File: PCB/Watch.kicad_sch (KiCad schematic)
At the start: 47 parts, among them J1 USB_C_Receptacle_USB2.0_14P, Q1 2N3904, Q2 2N3904, Q3 2N3904, Q4 2N3904, SW1 SW_Push, SW3 SW_Push, SW4 SW_Push, U1 MCP73831-2-OT, U3 AP2112K-3.3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

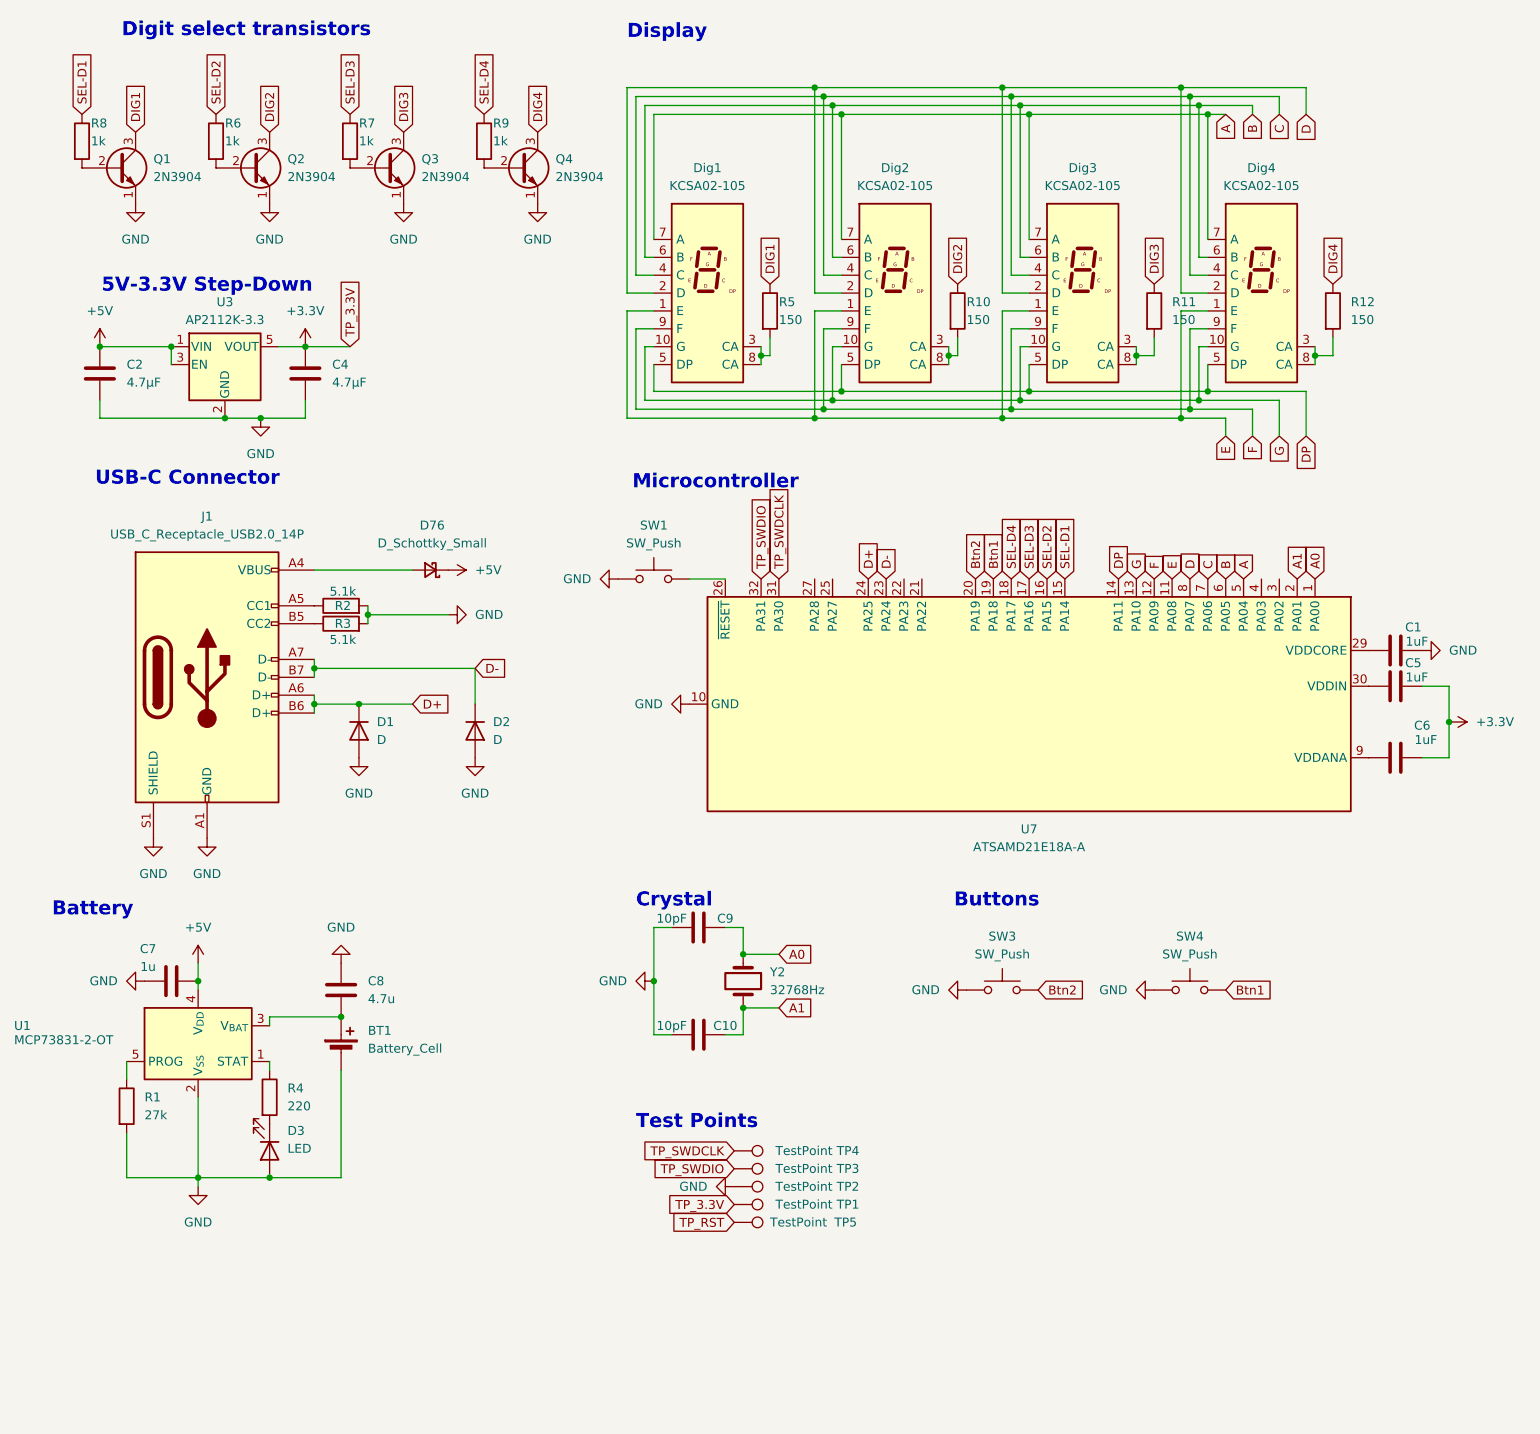
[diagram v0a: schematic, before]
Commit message: Switch regulator
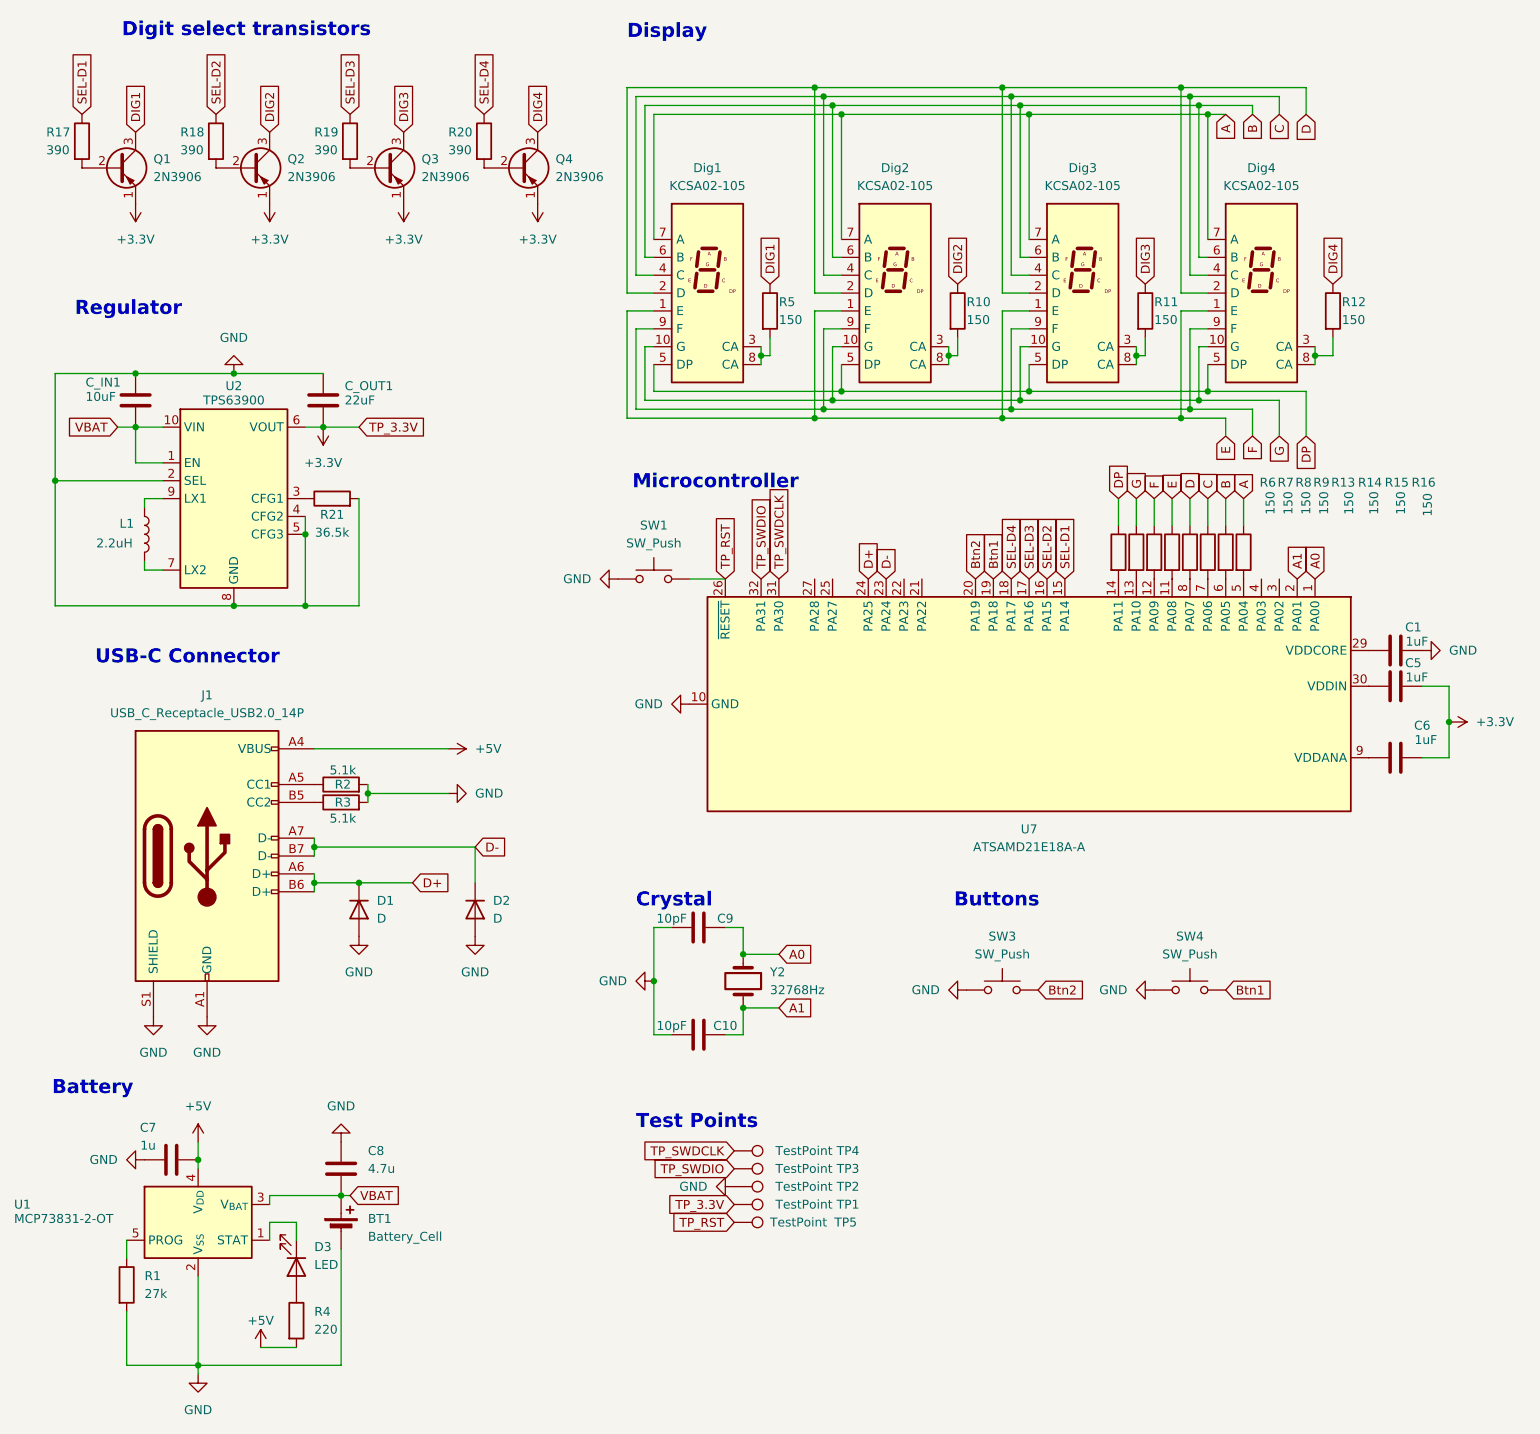
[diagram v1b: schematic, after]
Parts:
- removed C2, C4: 4.7µF, Capacitor_SMD:C_0603_1608Metric, symbol Device:C
- removed D76: D_Schottky_Small, Diode_SMD:D_SOD-323, symbol Device:D_Schottky_Small
- removed Q1, Q2, Q3, Q4: 2N3904, Package_TO_SOT_SMD:SOT-23, symbol Transistor_BJT:2N3904
- removed U3: AP2112K-3.3, Package_TO_SOT_SMD:SOT-23-5, symbol Regulator_Linear:AP2112K-3.3
- added C_IN1: 10uF, Capacitor_SMD:C_0603_1608Metric, symbol Device:C
- added C_OUT1: 22uF, Capacitor_SMD:C_0603_1608Metric, symbol Device:C
- added L1: 2.2uH, Inductor_SMD:L_0805_2012Metric, symbol Device:L
- added Q1, Q2, Q3, Q4: 2N3906, Package_TO_SOT_SMD:SOT-23, symbol Transistor_BJT:2N3906
- added R13, R14, R15, R16: 150, Resistor_SMD:R_0402_1005Metric, symbol Device:R
- added R17, R18, R19, R20: 390, Resistor_SMD:R_0402_1005Metric, symbol Device:R
- added R21: 36.5k, Resistor_SMD:R_0402_1005Metric, symbol Device:R
- added U2: TPS63900, Package_SON:WSON-10-1EP_2.5x2.5mm_P0.5mm_EP1.2x2mm_ThermalVias, symbol Regulator_Switching:TPS63900
- C1, C10, C5, C6, C7, C9: footprint Capacitor_SMD:C_0603_1608Metric -> Capacitor_SMD:C_0402_1005Metric
- D3: footprint LED_SMD:LED_0603_1608Metric -> LED_SMD:LED_0402_1005Metric
- R1, R10, R11, R12, R2, R3, R4, R5: footprint Resistor_SMD:R_0603_1608Metric -> Resistor_SMD:R_0402_1005Metric
- R6, R7, R8, R9: value 1k -> 150; footprint Resistor_SMD:R_0603_1608Metric -> Resistor_SMD:R_0402_1005Metric
- TP5: footprint (none) -> TestPoint:TestPoint_Pad_D1.0mm
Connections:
- net +3.3V: now also C_OUT1.2, Q1.1 (E), Q2.1 (E), Q3.1 (E), Q4.1 (E), U2.6 (VOUT)
- net +5V: now also J1.A4 (VBUS), J1.A9 (VBUS), J1.B4 (VBUS), J1.B9 (VBUS), R4.2
- net A: now also R16.1; no longer U7.5 (PA04)
- net B: now also R15.1; no longer U7.6 (PA05)
- net C: now also R14.1; no longer U7.7 (PA06)
- net D: now also R13.1; no longer U7.8 (PA07)
- net DIG1: now also Q1.3 (C)
- net DIG2: now also Q2.3 (C)
- net DIG3: now also Q3.3 (C)
- net DIG4: now also Q4.3 (C)
- net DP: now also R6.1; no longer U7.14 (PA11)
- net E: now also R9.1; no longer U7.11 (PA08)
- net F: now also R8.1; no longer U7.12 (PA09)
- net G: now also R7.1; no longer U7.13 (PA10)
- net GND: now also C_IN1.1, C_OUT1.1, R21.2, U2.11 (GND), U2.2 (SEL), U2.4 (CFG2), U2.5 (CFG3), U2.8 (GND); no longer D3.2 (A)
- net SEL-D1: now also R17.1; no longer R8.1
- net SEL-D2: now also R18.1; no longer R6.1
- net SEL-D3: now also R19.1; no longer R7.1
- net SEL-D4: now also R20.1; no longer R9.1
- net TP_RST: now also SW1.2, U7.26 (~{RESET})
- net at D3.1 (K): now also U1.1 (STAT); no longer R4.2
- net at R9.2: now also U7.11 (PA08)
- net VBAT: now reaches BT1.1 (+), C8.2, U1.3 (V_{BAT})
- net VBAT: now also C_IN1.2, U2.1 (EN), U2.10 (VIN)
- net at R6.2: now also U7.14 (PA11)
- net at R7.2: now also U7.13 (PA10)
- net at R8.2: now also U7.12 (PA09)
- net at R4.1: now also D3.2 (A); no longer U1.1 (STAT)
- new net: L1.1, U2.9 (LX1)
- new net: L1.2, U2.7 (LX2)
- new net: R14.2, U7.7 (PA06)
- new net: Q1.2 (B), R17.2
- new net: R13.2, U7.8 (PA07)
- new net: R15.2, U7.6 (PA05)
- new net: Q4.2 (B), R20.2
- new net: R21.1, U2.3 (CFG1)
- new net: R16.2, U7.5 (PA04)
- new net: Q3.2 (B), R19.2
- new net: Q2.2 (B), R18.2
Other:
- note added: "Regulator"
- note removed: "5V-3.3V Step-Down"
- moved on the sheet: BT1, C7, C8, D1, D2, D3, J1, R1, R11, R2, R3, R4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

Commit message: Fix charge LED, display resistors
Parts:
- removed R10, R11, R12, R5: 150, Resistor_SMD:R_0402_1005Metric, symbol Device:R
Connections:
- net DIG1: now also Dig1.3 (CA), Dig1.8 (CA)
- net DIG2: now also Dig2.3 (CA), Dig2.8 (CA)
- net DIG3: now also Dig3.3 (CA), Dig3.8 (CA)
- net DIG4: now also Dig4.3 (CA), Dig4.8 (CA)
- net at D3.1 (K): now also R4.1; no longer U1.1 (STAT)
- net at D3.2 (A): now also U1.1 (STAT); no longer R4.1
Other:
- moved on the sheet: D3, R4

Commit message: Add resistor to reset button, small schematic changes
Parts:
- added R5: 10k, Resistor_SMD:R_0402_1005Metric, symbol Device:R
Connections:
- net TP_RST: now also R5.2; no longer SW1.2
- new net: R5.1, SW1.2
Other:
- company: (none) -> Daniel Benge
- moved on the sheet: SW1
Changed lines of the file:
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@@
 	(title_block
 		(title "Watch PCB")
-		(date "2025-04-29")
-		(rev "0.9")
+		(date "2025-06-11")
+		(rev "1.0")
+		(company "Daniel Benge")
 	)
 	(junction
@@
 	(wire
 		(pts
+			(xy 161.29 148.59) (xy 170.18 148.59)
+		)
+		(stroke
+			(width 0)
+			(type default)
+		)
+	)
+	(wire
+		(pts
 			(xy 86.36 119.38) (xy 100.33 119.38)
 		)
@@
 	(wire
 		(pts
-			(xy 165.1 148.59) (xy 170.18 148.59)
-		)
-		(stroke
-			(width 0)
-			(type default)
-		)
-	)
-	(wire
-		(pts
 			(xy 156.21 78.74) (xy 182.88 78.74)
 		)
@@
 	(symbol
 		(lib_id "Switch:SW_Push")
-		(at 160.02 148.59 0)
+		(at 148.59 148.59 0)
 		(unit 1)
 		(exclude_from_sim no)
@@
 		(fields_autoplaced yes)
 		(property "Reference" "SW1"
-			(at 160.02 140.97 0)
+			(at 148.59 140.97 0)
 			(effects
 				(font
@@
 		)
 		(property "Value" "SW_Push"
-			(at 160.02 143.51 0)
+			(at 148.59 143.51 0)
 			(effects
 				(font
@@
 		)
 		(property "Footprint" "Button_Switch_SMD:SW_SPST_B3U-1000P"
-			(at 160.02 143.51 0)
+			(at 148.59 143.51 0)
 			(effects
 				(font
@@
 		)
 		(property "Datasheet" "~"
-			(at 160.02 143.51 0)
+			(at 148.59 143.51 0)
 			(effects
 				(font
@@
 		)
 		(property "Description" "Push button switch, generic, two pins"
-			(at 160.02 148.59 0)
+			(at 148.59 148.59 0)
 			(effects
 				(font
@@
 	)
 	(symbol
+		(lib_id "Device:R")
+		(at 157.48 148.59 90)
+		(unit 1)
+		(exclude_from_sim no)
+		(in_bom yes)
+		(on_board yes)
+		(dnp no)
+		(fields_autoplaced yes)
+		(property "Reference" "R5"
+			(at 157.48 142.24 90)
+			(effects
+				(font
+					(size 1.27 1.27)
+				)
+			)
+		)
+		(property "Value" "10k"
+			(at 157.48 144.78 90)
+			(effects
+				(font
+					(size 1.27 1.27)
+				)
+			)
+		)
+		(property "Footprint" "Resistor_SMD:R_0402_1005Metric"
+			(at 157.48 150.368 90)
+			(effects
+				(font
+					(size 1.27 1.27)
+				)
+				(hide yes)
+			)
+		)
+		(property "Datasheet" "~"
+			(at 157.48 148.59 0)
+			(effects
+				(font
+					(size 1.27 1.27)
+				)
+				(hide yes)
+			)
+		)
+		(property "Description" "Resistor"
+			(at 157.48 148.59 0)
+			(effects
+				(font
+					(size 1.27 1.27)
+				)
+				(hide yes)
+			)
+		)
+		(pin "2"
+		)
+		(pin "1"
+		)
+		(instances
+			(project ""
+				(path "/e5022d08-9dda-4e3a-b81c-bab3a6fb67af"
+					(reference "R5")
+					(unit 1)
+				)
+			)
+		)
+	)
+	(symbol
 		(lib_id "Device:D")
 		(at 118.11 195.58 270)
@@
 	(symbol
 		(lib_id "power:GND")
-		(at 154.94 148.59 270)
+		(at 143.51 148.59 270)
 		(unit 1)
 		(exclude_from_sim no)
@@
 		(dnp no)
 		(property "Reference" "#PWR09"
-			(at 148.59 148.59 0)
+			(at 137.16 148.59 0)
 			(effects
 				(font
@@
 		)
 		(property "Value" "GND"
-			(at 151.13 148.5899 90)
+			(at 139.7 148.5899 90)
 			(effects
 				(font
@@
 		)
 		(property "Footprint" ""
-			(at 154.94 148.59 0)
+			(at 143.51 148.59 0)
 			(effects
 				(font
@@
 		)
 		(property "Datasheet" ""
-			(at 154.94 148.59 0)
+			(at 143.51 148.59 0)
 			(effects
 				(font
@@
 		)
 		(property "Description" "Power symbol creates a global label with name \"GND\" , ground"
-			(at 154.94 148.59 0)
+			(at 143.51 148.59 0)
 			(effects
 				(font
